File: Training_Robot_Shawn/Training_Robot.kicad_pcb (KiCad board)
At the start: 4 copper layers, 94.5 x 89 mm, 32 parts, among them J1 Conn_01x04_Pin, J2 Conn_01x04_Pin, J3 Conn_01x04_Pin, J4 Conn_01x02_Pin, J5 Conn_01x02_Pin, J6 Conn_01x08_Socket, M1 FrontL, M2 FrontR, M3 BackL, M4 BackR, SW1 SW_SPDT_312, U3 ESP32-S3-DevKitC

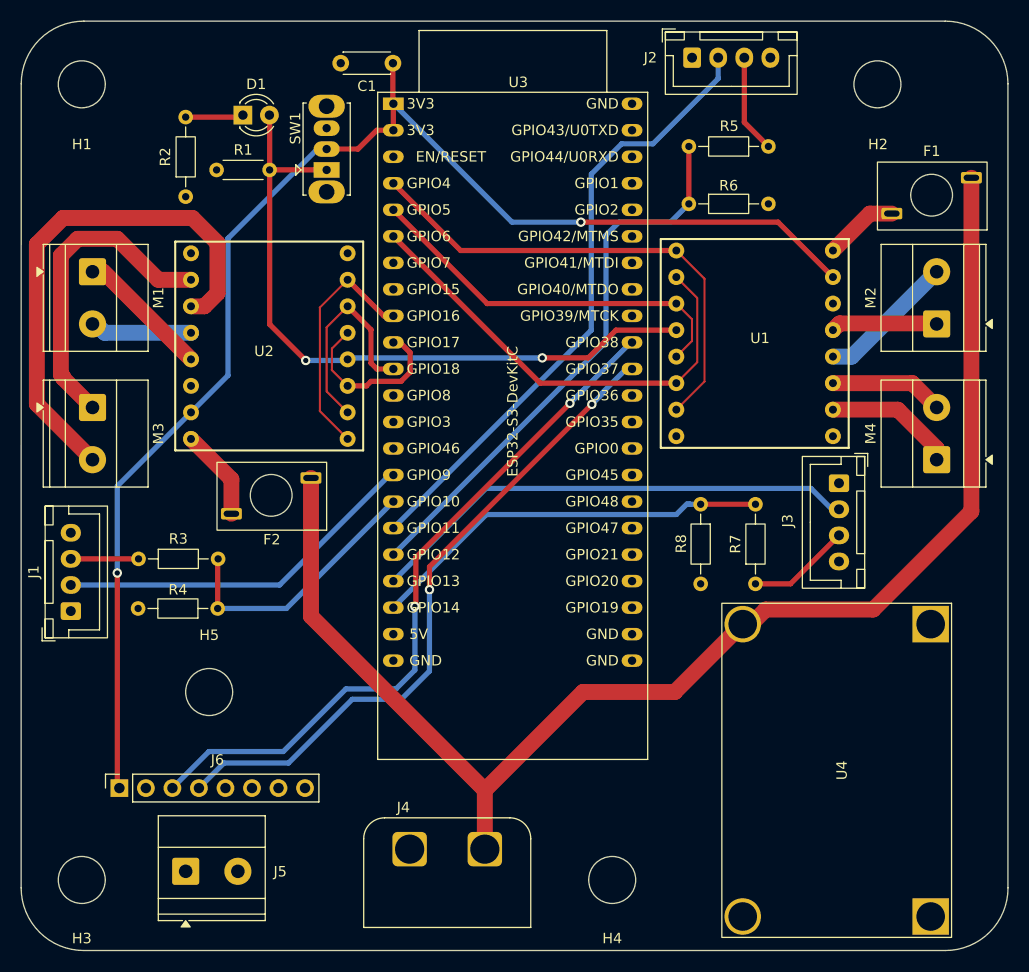
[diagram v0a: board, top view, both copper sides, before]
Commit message: flip fuse footprint, connect esp 5v/gnd pins to board, remove buck converter
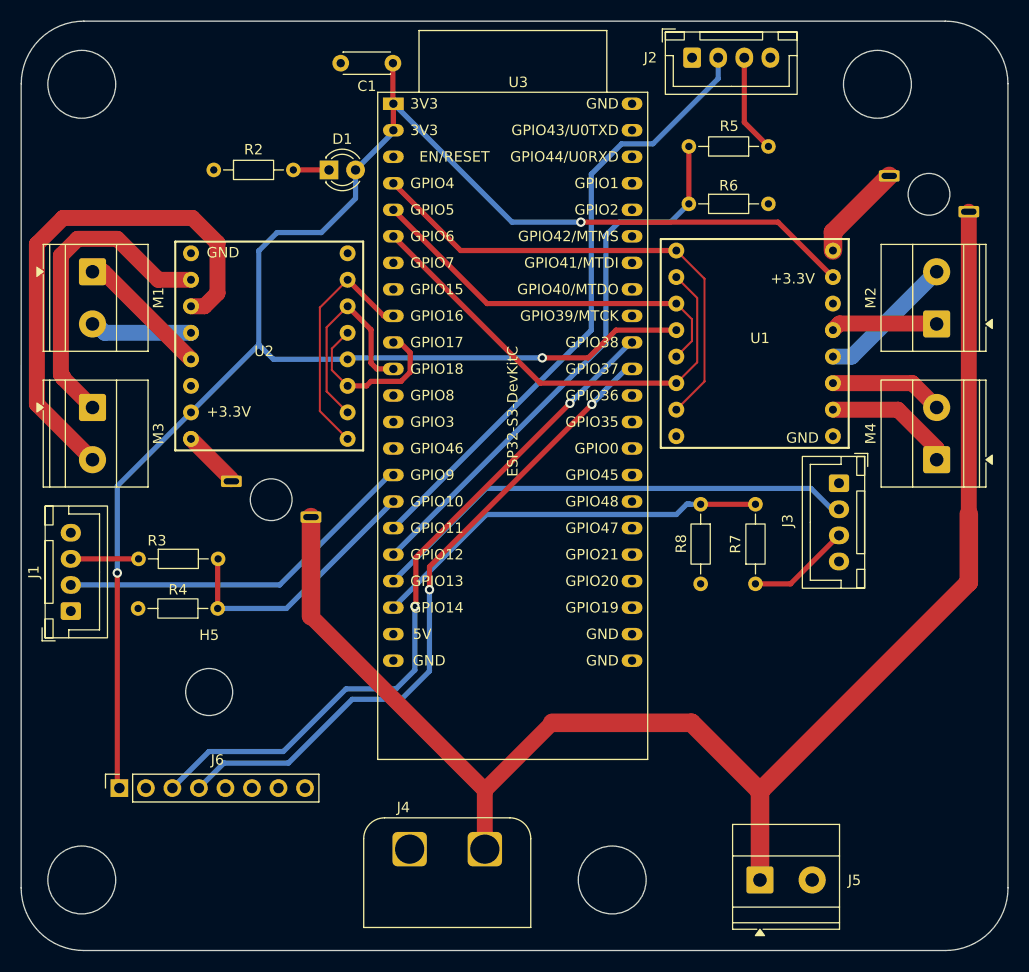
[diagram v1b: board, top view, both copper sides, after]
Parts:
- removed R1: 10K, Resistor_THT:R_Axial_DIN0204_L3.6mm_D1.6mm_P5.08mm_Horizontal
- removed SW1: SW_SPDT_312, Button_Switch_THT:SW_Slide_SPDT_Straight_CK_OS102011MS2Q
- removed U4: ~, MARS Custom Footprints:MP1495 Buck Converter
- F1, F2: moved to B.Cu
- H1, H2, H3, H4: footprint MountingHole:MountingHole_4.5mm -> MountingHole:MountingHole_6.5mm
- moved J5 55.0 mm to (204.8, 129.0)
- moved D1 9.78 mm to (163.5, 61.0)
- moved F2 3.75 mm to (161.8, 94.2)
- moved R2 3.71 mm to (152.4, 61.0), turned to 0 degrees
- moved F1 3.26 mm to (224.8, 65.0)
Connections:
- D1 pad 2: /STBY -> +3V3
- J5 pad 1: +5V -> +12V
- U1 pad 4: /STBY -> +3V3
- U2 pad 4: /STBY -> +3V3
- U3 pad 21: unconnected-(U3-5V-Pad21) -> +5V
- U3 pad 22: unconnected-(U3-GND-Pad22)_2 -> GND
- U3 pad 23: unconnected-(U3-GND-Pad22)_1 -> GND
- U3 pad 24: unconnected-(U3-GND-Pad22) -> GND
- U3 pad 44: unconnected-(U3-GND-Pad22)_3 -> GND
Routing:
- net /STBY: track 67.2 -> 0.00 mm, vias 2 -> 0
- net +3V3: track 132.7 -> 173.8 mm, vias 2 -> 3
- net +12V: track 132.1 -> 142.7 mm
- net Net-(U2-VM): track 8.77 -> 5.47 mm
- net Net-(U1-VM): track 7.11 -> 9.38 mm
- net Net-(D1-K): track 5.56 -> 3.42 mm
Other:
- board text added: "+3.3V"
- board text added: "GND"

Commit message: Small changes before second order
-Added silkscreen text for pins on each motor controller
-Slightly adjusted layouts of right JST connector, bypass capacitor, some vias, and some traces
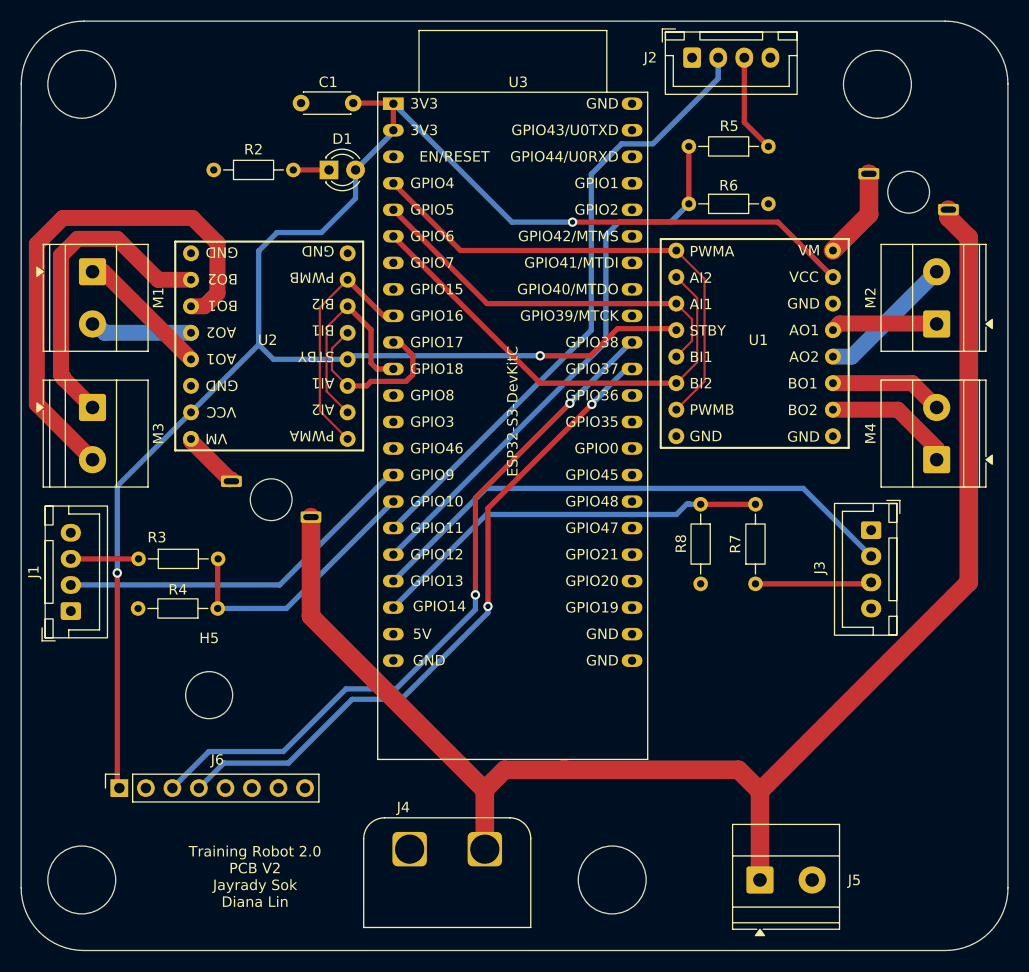
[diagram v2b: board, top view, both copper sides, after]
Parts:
- H3, H4: moved to B.Cu
- moved H3 50.8 mm to (190.6, 129.0), turned to 180 degrees
- moved H4 50.8 mm to (139.8, 129.0), turned to 180 degrees
- moved F1 6.02 mm to (219.1, 63.0)
- moved J3 5.45 mm to (215.4, 95.5)
- moved C1 5.39 mm to (165.8, 54.6)
- moved F2 4.14 mm to (158.0, 92.5)
- moved H5 0.30 mm to (152.0, 111.3)
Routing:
- net /R_US_TRIG: track 47.2 -> 52.1 mm
- net +12V: track 142.7 -> 140.1 mm
- net Net-(J3-Pin_3): track 9.92 -> 11.1 mm
- net Net-(U1-VM): track 9.38 -> 8.79 mm
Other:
- board text added: "AI1"
- board text added: "AI2"
- board text added: "AO1"
- board text added: "AO2"
- board text added: "BI1"
- board text added: "BI2"
- board text added: "BO1"
- board text added: "BO2"
- board text added: "PWMA"
- board text added: "PWMB"
- board text added: "STBY"
- board text added: "Training Robot 2.0 PCB V2 Jayrady Sok Diana Lin"
- board text added: "VCC"
- board text added: "VM"
- board text removed: "+3.3V"

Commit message: another final change before second order
-swapped pins on xt60 connector footprint.
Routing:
- net +12V: track 140.1 -> 144.1 mm
